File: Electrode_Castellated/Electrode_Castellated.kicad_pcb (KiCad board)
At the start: 4 copper layers, 75 x 25 mm, 21 parts, among them J1 Connector

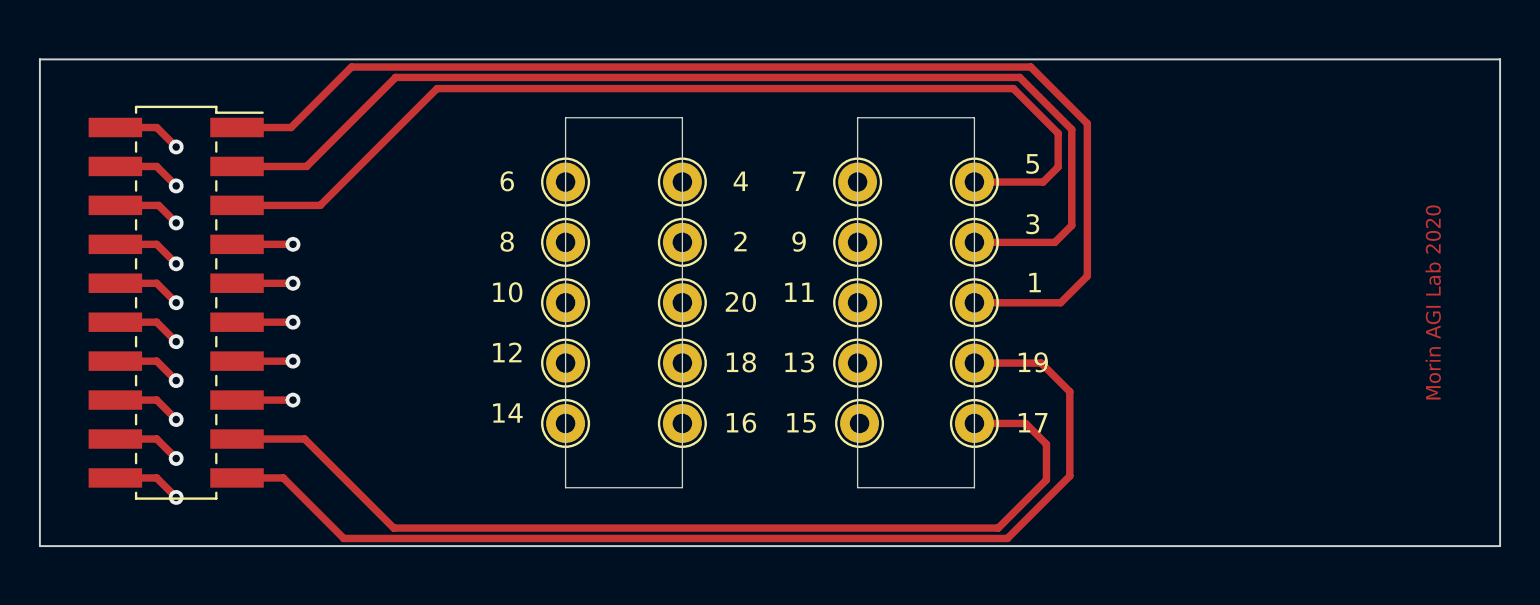
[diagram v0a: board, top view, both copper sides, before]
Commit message: Switch to pogo pin style connector pads
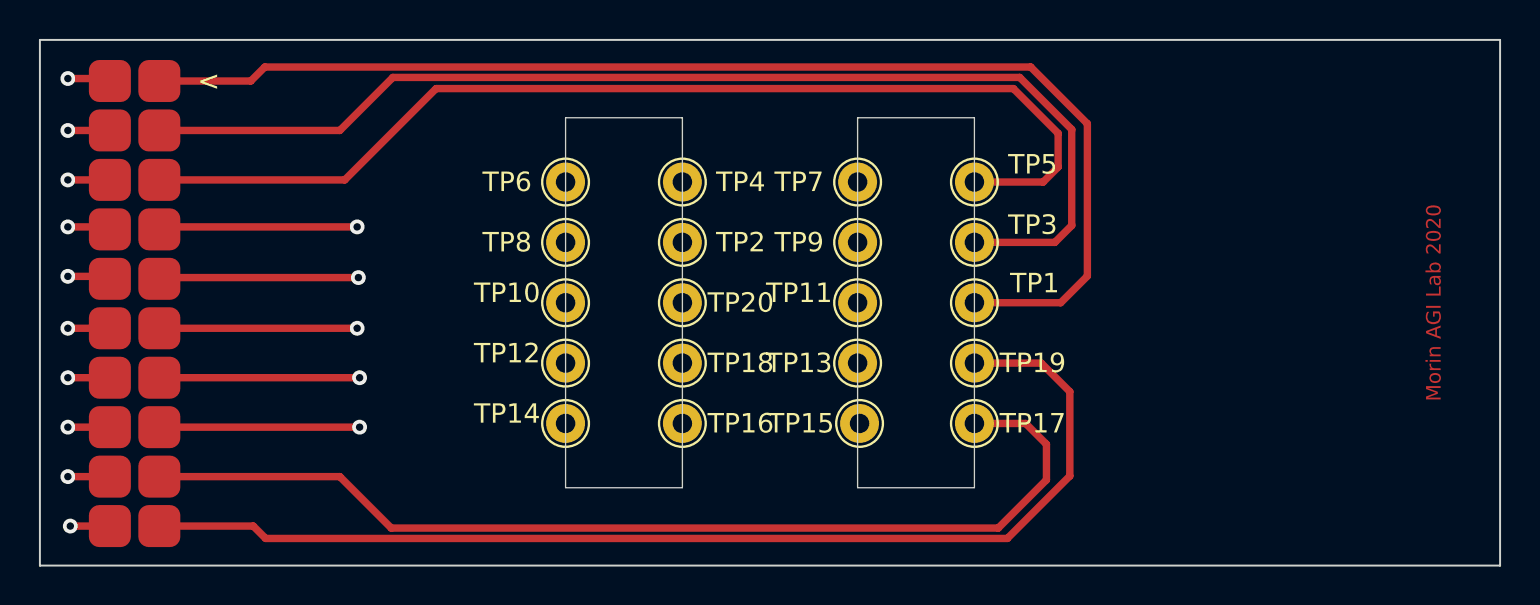
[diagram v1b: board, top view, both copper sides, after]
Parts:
- removed J1: Connector, Connector_PinSocket_2.00mm:PinSocket_2x10_P2.00mm_Vertical_SMD
- added <: Connector, eaton:Millmax Pad Contacts, F.Cu at (54.9, 137.5)
- TP20: renamed from 20; value 20 -> 30
- renumbered 1 to TP1, 10 to TP10, 11 to TP11, 12 to TP12, 13 to TP13, 14 to TP14, 15 to TP15, 16 to TP16, 17 to TP17, 18 to TP18, 19 to TP19, 2 to TP2, 3 to TP3, 4 to TP4, 5 to TP5, 6 to TP6, 7 to TP7, 8 to TP8, 9 to TP9
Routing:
- net Net-(J1-Pad10): track 23.4 -> 28.2 mm
- net Net-(J1-Pad12): track 23.8 -> 28.5 mm
- net Net-(J1-Pad8): track 23.8 -> 28.4 mm
- net Net-(J1-Pad6): track 24.1 -> 28.4 mm
- net Net-(J1-Pad4): track 43.4 -> 47.5 mm
- net Net-(J1-Pad20): track 50.2 -> 54.2 mm
- net Net-(J1-Pad9): track 40.6 -> 44.6 mm
- net Net-(J1-Pad2): track 49.3 -> 53.3 mm
- net Net-(J1-Pad16): track 42.0 -> 46.0 mm
- net Net-(J1-Pad14): track 24.4 -> 28.3 mm
- net Net-(J1-Pad18): track 46.3 -> 50.2 mm
- net Net-(J1-Pad11): track 44.1 -> 48.0 mm
- net Net-(J1-Pad7): track 37.6 -> 41.5 mm
- net Net-(J1-Pad13): track 41.6 -> 45.2 mm
- net Net-(J1-Pad5): track 52.0 -> 55.4 mm
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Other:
- board size 75 x 25 mm -> 75 x 27 mm

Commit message: Fix silkscreen labels, add dimensions & SN
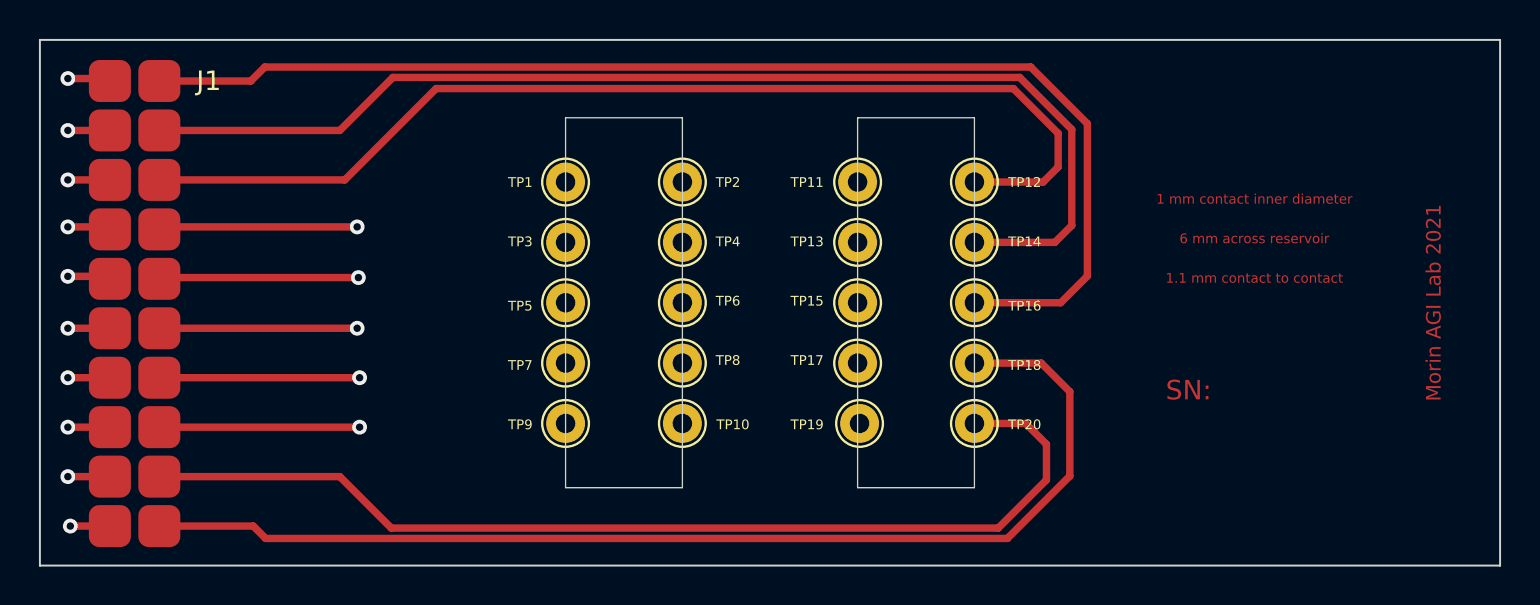
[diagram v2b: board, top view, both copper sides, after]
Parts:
- renumbered < to J1, TP6 to TP1, TP16 to TP10, TP7 to TP11, TP5 to TP12, TP9 to TP13, TP3 to TP14, TP11 to TP15, TP1 to TP16, TP13 to TP17, TP19 to TP18, TP15 to TP19, TP4 to TP2, TP17 to TP20, TP8 to TP3, TP2 to TP4, TP10 to TP5, TP20 to TP6, TP12 to TP7, TP18 to TP8, TP14 to TP9
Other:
- board text added: "1 mm contact inner diameter"
- board text added: "1.1 mm contact to contact"
- board text added: "6 mm across reservoir"
- board text added: "Morin AGI Lab 2021"
- board text added: "SN:"
- board text removed: "Morin AGI Lab 2020"
